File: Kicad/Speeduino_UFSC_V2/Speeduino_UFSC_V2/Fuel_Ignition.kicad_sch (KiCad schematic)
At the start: 19 parts, among them Q1 Q_NMOS_GDS, U1 TC4424A

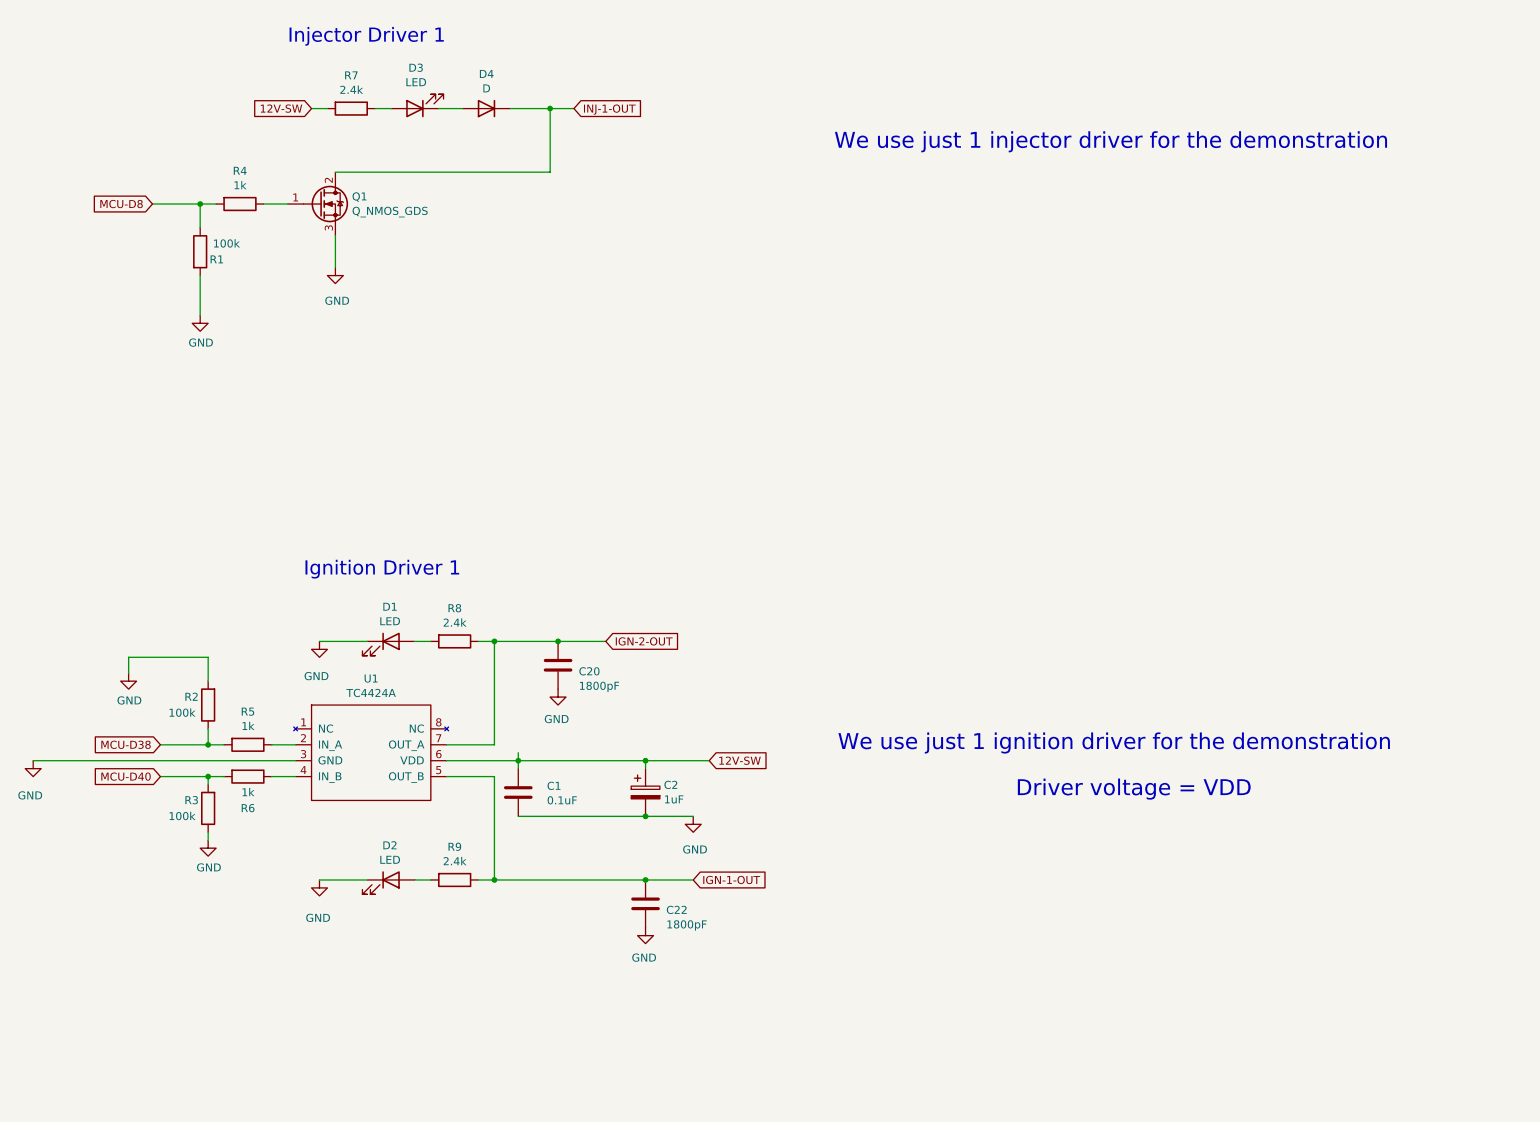
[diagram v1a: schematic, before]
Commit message: Add 2 injectors in schematic
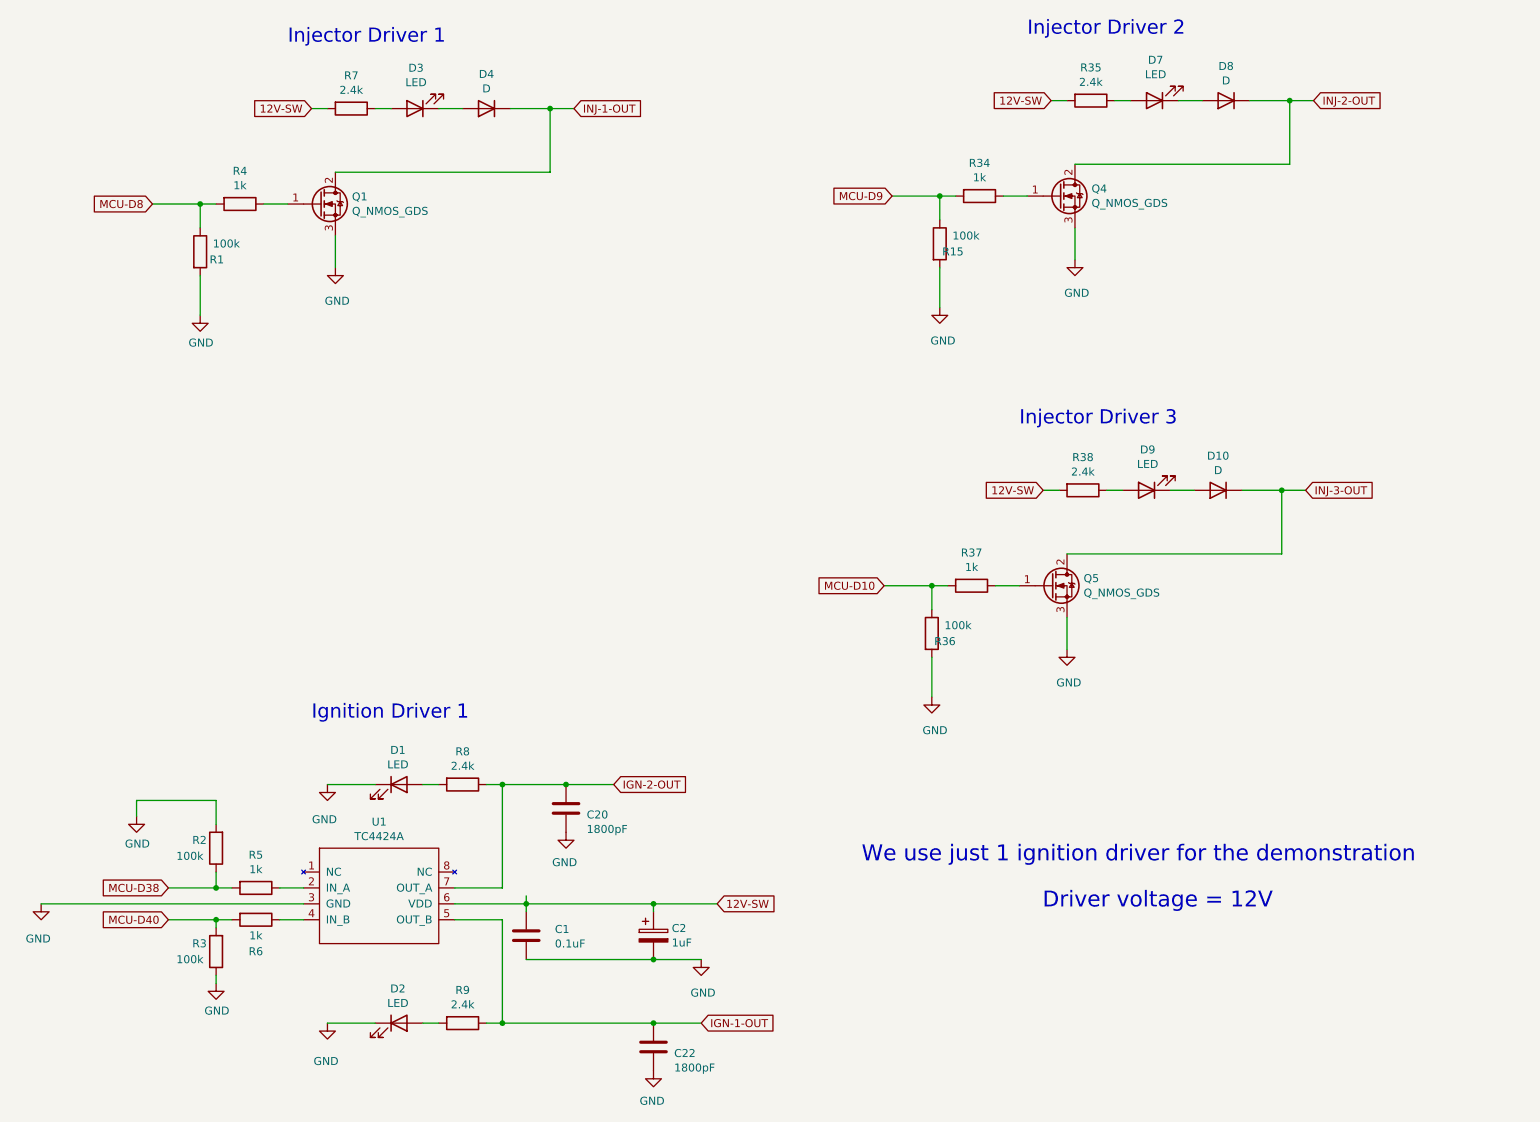
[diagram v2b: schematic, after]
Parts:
- added D10, D8: D, Diode_THT:D_DO-35_SOD27_P7.62mm_Horizontal, symbol Device:D
- added D7, D9: LED, LED_THT:LED_D3.0mm, symbol Device:LED
- added Q4, Q5: Q_NMOS_GDS, Package_TO_SOT_THT:TO-220-3_Horizontal_TabDown, symbol Device:Q_NMOS_GDS
- added R15, R36: 100k, Resistor_THT:R_Axial_DIN0204_L3.6mm_D1.6mm_P5.08mm_Horizontal, symbol Device:R
- added R34, R37: 1k, Resistor_THT:R_Axial_DIN0204_L3.6mm_D1.6mm_P5.08mm_Horizontal, symbol Device:R
- added R35, R38: 2.4k, Resistor_THT:R_Axial_DIN0204_L3.6mm_D1.6mm_P5.08mm_Horizontal, symbol Device:R
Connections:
- net 12V-SW: now also R35.2, R38.2
- net GND: now also Q4.3 (S), Q5.3 (S), R15.2, R36.2
- new net: Q5.1 (G), R37.1
- new net: Q4.1 (G), R34.1
- new net: D10.2 (A), D9.1 (K)
- new net: D9.2 (A), R38.1
- new net: D7.2 (A), R35.1
- new net: D7.1 (K), D8.2 (A)
- new net INJ-2-OUT: D8.1 (K), Q4.2 (D)
- new net INJ-3-OUT: D10.1 (K), Q5.2 (D)
- new net MCU-D10: R36.1, R37.2
- new net MCU-D9: R15.1, R34.2
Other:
- note added: "Driver voltage = 12V"
- note added: "Injector Driver 2"
- note added: "Injector Driver 3"
- note removed: "Driver voltage = VDD"
- note removed: "We use just 1 injector driver for the demonstration"
- moved on the sheet: C1, C2, C20, C22, D1, D2, R2, R3, R5, R6, R8, R9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
